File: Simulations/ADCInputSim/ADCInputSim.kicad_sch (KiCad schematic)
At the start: 8 parts, among them U1 ${SIM.PARAMS}

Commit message: ADC driver dialed in
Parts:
- removed U1: ${SIM.PARAMS}, symbol Simulation_SPICE:OPAMP
- added C1: 1u, symbol Device:C
- added D1, D2: D, symbol Simulation_SPICE:D
- added R5: 10k, symbol Device:R_US
- added R6: 680k, symbol Device:R_US
- added R7, R8, R9: 100k, symbol Device:R_US
- added U1: LM324, symbol Amplifier_Operational:LM324
- added V3: VSIN, symbol Simulation_SPICE:VSIN
- R1: value 100k -> 56k
- R2: value 100k -> 47k
- R3: value 51k -> 47k
- R4: value 27k -> 22k
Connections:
- net +18V: now also U1.4 (V+)
- net EnvOut: now also U1.7
- net GND: now also U1.11 (V-), V3.2
- net VG: now also C1.2, U1.3 (+)
- net vMirror: now reaches R3.2, R4.2
- net vMirror: now also U1.10 (+), U1.5 (+)
- net at R1.2, R2.1: now also U1.6 (-)
- new net: R8.1, U1.13 (-), U1.14
- new net: R8.2, R9.1, U1.9 (-)
- new net: D2.2 (A), R6.2, R7.1, U1.2 (-)
- new net: D1.2 (A), D2.1 (K), U1.1
- new net Rect: D1.1 (K), R5.1, R6.1
- new net SigOut: R7.2, V3.1
- new net VUcap: C1.1, R5.2, U1.12 (+)
- new net VUout: R9.2, U1.8
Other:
- note added: "Expect a max of ~1.2-1.5 Vpp here"

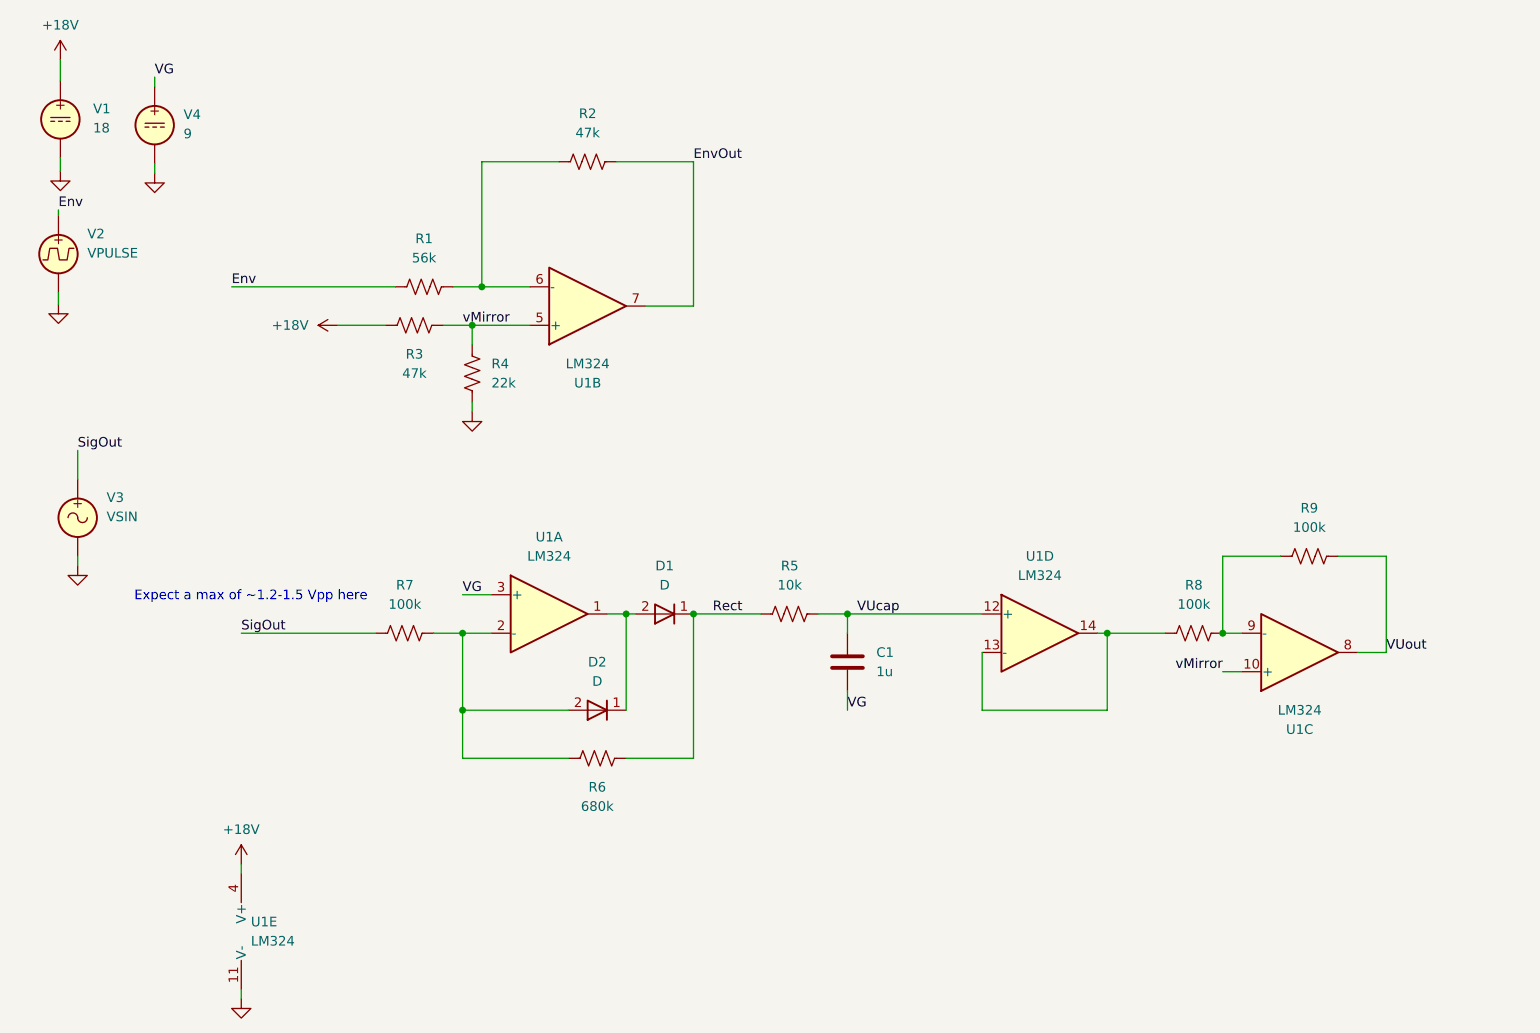
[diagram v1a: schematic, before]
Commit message: switched to NCS2007x op-amp
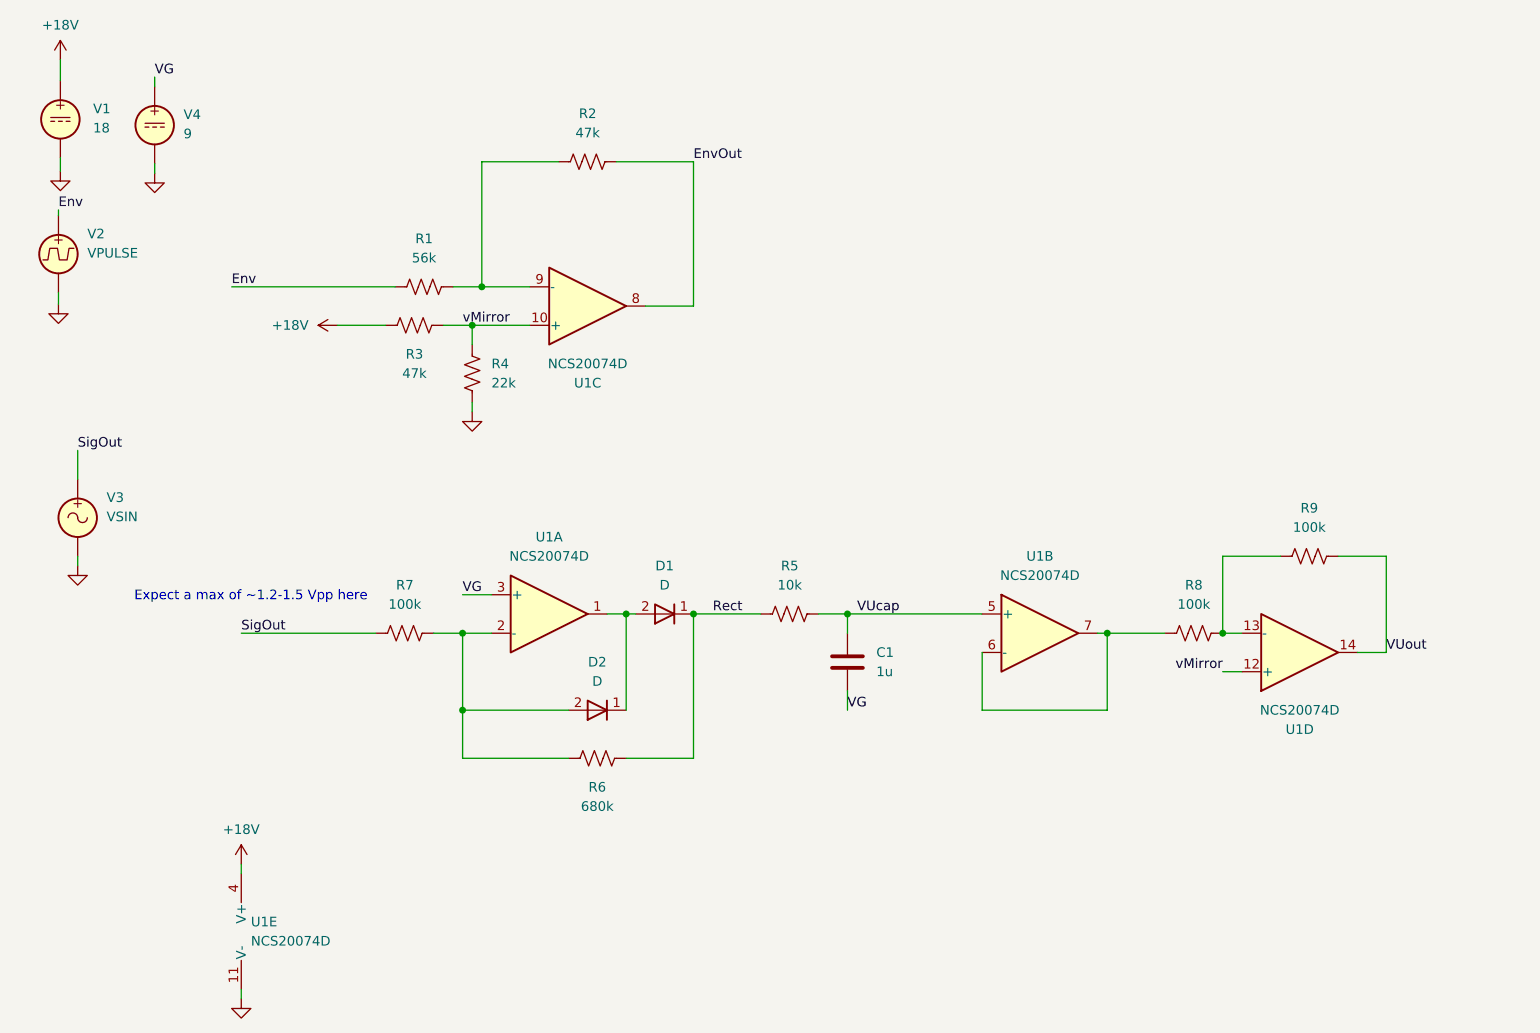
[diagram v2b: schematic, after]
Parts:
- removed U1: LM324, symbol Amplifier_Operational:LM324
- added U1: NCS20074D, Package_SO:SOIC-14_3.9x8.7mm_P1.27mm, symbol Amplifier_Operational:NCS20074D
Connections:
- net +18V: now also U1.4 (V+)
- net EnvOut: now also U1.8
- net GND: now also U1.11 (V-)
- net VG: now also U1.3 (+)
- net VUcap: now also U1.5 (+)
- net VUout: now also U1.14
- net vMirror: now also U1.10 (+), U1.12 (+)
- net at R8.1: now also U1.6 (-), U1.7
- net at R8.2, R9.1: now also U1.13 (-)
- net at D2.2 (A), R6.2, R7.1: now also U1.2 (-)
- net at D1.2 (A), D2.1 (K): now also U1.1
- net at R1.2, R2.1: now also U1.9 (-)

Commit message: basic firmware
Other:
- moved on the sheet: U1E
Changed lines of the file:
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@@
 	(wire
 		(pts
-			(xy 49.53 139.7) (xy 49.53 140.97)
+			(xy 129.54 73.66) (xy 129.54 74.93)
 		)
 		(stroke
@@
 	(wire
 		(pts
-			(xy 49.53 156.21) (xy 49.53 157.48)
+			(xy 129.54 90.17) (xy 129.54 91.44)
 		)
 		(stroke
@@
 	(symbol
 		(lib_id "power:GND")
-		(at 49.53 157.48 0)
+		(at 129.54 91.44 0)
 		(unit 1)
 		(body_style 1)
@@
 		(fields_autoplaced yes)
 		(property "Reference" "#PWR015"
-			(at 49.53 163.83 0)
+			(at 129.54 97.79 0)
 			(hide yes)
 			(show_name no)
@@
 		)
 		(property "Value" "GND"
-			(at 49.53 161.29 0)
+			(at 129.54 95.25 0)
 			(hide yes)
 			(show_name no)
@@
 		)
 		(property "Footprint" ""
-			(at 49.53 157.48 0)
+			(at 129.54 91.44 0)
 			(hide yes)
 			(show_name no)
@@
 		)
 		(property "Datasheet" ""
-			(at 49.53 157.48 0)
+			(at 129.54 91.44 0)
 			(hide yes)
 			(show_name no)
@@
 		)
 		(property "Description" "Power symbol creates a global label with name \"GND\" , ground"
-			(at 49.53 157.48 0)
+			(at 129.54 91.44 0)
 			(hide yes)
 			(show_name no)
@@
 	(symbol
 		(lib_id "power:+18V")
-		(at 49.53 139.7 0)
+		(at 129.54 73.66 0)
 		(unit 1)
 		(body_style 1)
@@
 		(fields_autoplaced yes)
 		(property "Reference" "#PWR014"
-			(at 49.53 143.51 0)
+			(at 129.54 77.47 0)
 			(hide yes)
 			(show_name no)
@@
 		)
 		(property "Value" "+18V"
-			(at 49.53 135.128 0)
+			(at 129.54 69.088 0)
 			(show_name no)
 			(do_not_autoplace no)
@@
 		)
 		(property "Footprint" ""
-			(at 49.53 139.7 0)
+			(at 129.54 73.66 0)
 			(hide yes)
 			(show_name no)
@@
 		)
 		(property "Datasheet" ""
-			(at 49.53 139.7 0)
+			(at 129.54 73.66 0)
 			(hide yes)
 			(show_name no)
@@
 		)
 		(property "Description" "Power symbol creates a global label with name \"+12V\""
-			(at 49.53 139.7 0)
+			(at 129.54 73.66 0)
 			(hide yes)
 			(show_name no)
@@
 	(symbol
 		(lib_id "Amplifier_Operational:NCS20074D")
-		(at 49.53 148.59 0)
+		(at 129.54 82.55 0)
 		(unit 5)
 		(body_style 1)
@@
 		(fields_autoplaced yes)
 		(property "Reference" "U1"
-			(at 50.8 147.3199 0)
+			(at 130.81 81.2799 0)
 			(show_name no)
 			(do_not_autoplace no)
@@
 		)
 		(property "Value" "NCS20074D"
-			(at 50.8 149.8599 0)
+			(at 130.81 83.8199 0)
 			(show_name no)
 			(do_not_autoplace no)
@@
 		)
 		(property "Footprint" "Package_SO:SOIC-14_3.9x8.7mm_P1.27mm"
-			(at 52.07 148.59 0)
+			(at 132.08 82.55 0)
 			(hide yes)
 			(show_name no)
@@
 		)
 		(property "Datasheet" "https://www.onsemi.com/pub/Collateral/NCS20071-D.PDF"
-			(at 55.88 144.78 0)
+			(at 135.89 78.74 0)
 			(hide yes)
 			(show_name no)
@@
 		)
 		(property "Description" "Quad, 2.8V/µs, Rail-to-Rail Output, SOIC-14"
-			(at 49.53 148.59 0)
+			(at 129.54 82.55 0)
 			(hide yes)
 			(show_name no)
@@
 		)
 		(property "Sim.Library" "NCS2007X.MOD"
-			(at 49.53 148.59 0)
+			(at 129.54 82.55 0)
 			(hide yes)
 			(show_name no)
@@
 		)
 		(property "Sim.Name" "NCS2007_Quad"
-			(at 49.53 148.59 0)
+			(at 129.54 82.55 0)
 			(hide yes)
 			(show_name no)
@@
 		)
 		(property "Sim.Device" "SUBCKT"
-			(at 49.53 148.59 0)
+			(at 129.54 82.55 0)
 			(hide yes)
 			(show_name no)
@@
 		)
 		(property "Sim.Pins" "1=1 2=2 3=3 4=4 5=5 6=6 7=7 8=8 9=9 10=10 11=11 12=12 13=13 14=14"
-			(at 49.53 148.59 0)
-			(hide yes)
-			(show_name no)
+			(at 129.54 82.55 0)
+			(hide yes)
+			(show_name no)

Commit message: updated env. follower and ADC driver in schem
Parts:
- removed D2: D, symbol Simulation_SPICE:D
- added C2: 22n, symbol Device:C
- added R10: 47k, symbol Device:R_US
- added R11: 22k, symbol Device:R_US
- C1: value 1u -> 470n
- R2: value 47k -> 56k
- R3: value 47k -> 91k
- R4: value 22k -> 47k
- R5: value 10k -> 1k
- R6: value 680k -> 220
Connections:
- net Rect: now also U1.2 (-); no longer R6.1
- net SigOut: now also U1.3 (+); no longer R7.2
- net VG: now also R7.1, R11.1; no longer U1.3 (+)
- net VUcap: now also R7.2
- net VUout: now also C2.2
- net CapGain: now reaches R8.1, U1.7
- net CapGain: now also R10.2; no longer U1.6 (-)
- net at R8.2, R9.1, U1.13 (-): now also C2.1
- net at D1.2 (A): now also R6.1; no longer U1.1
- new net: R6.2, U1.1
- new net: R10.1, R11.2, U1.6 (-)
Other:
- note added: ".PARAM inputAmp = 0.7"
- moved on the sheet: D1, R6, R8, R9, U1A, U1B, U1D
